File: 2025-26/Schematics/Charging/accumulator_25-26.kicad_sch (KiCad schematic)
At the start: 20 parts, among them J1 Conn_02x06_Counter_Clockwise, J2 Conn_02x06_Counter_Clockwise, K1 GV24 1BAX, K3 P115 BDA, K4 GV24 1BAX, U3 RSB, U5 Volt_indic

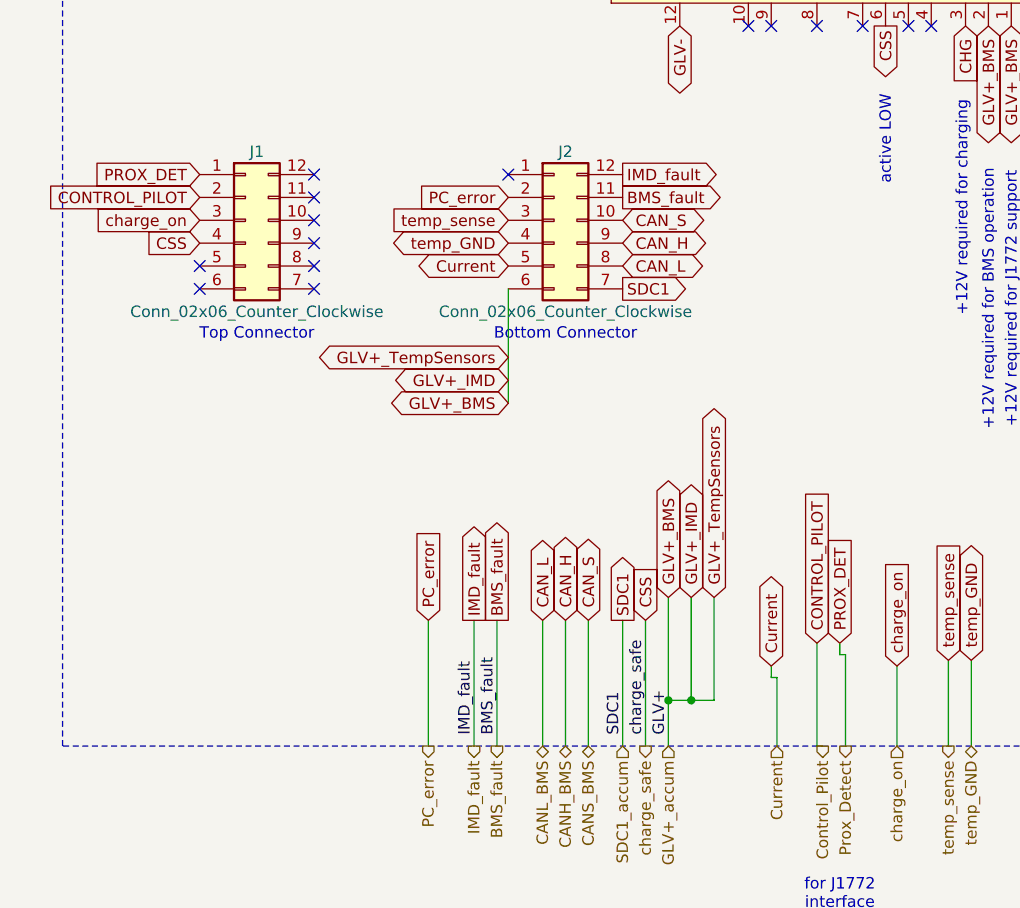
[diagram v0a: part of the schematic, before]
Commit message: updates to accumulator sch
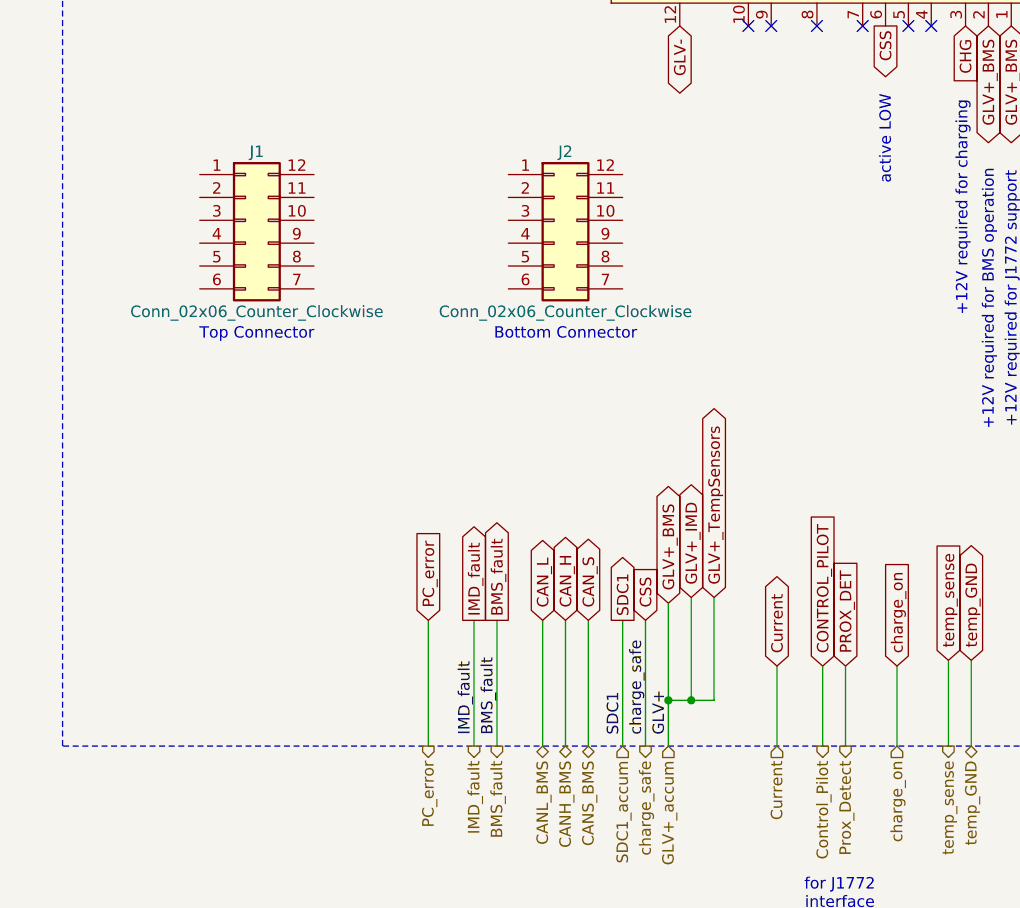
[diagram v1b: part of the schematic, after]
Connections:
- net BMS_fault: no longer J2.11 (Pin_11)
- net CAN_H: no longer J2.9 (Pin_9)
- net CAN_L: no longer J2.8 (Pin_8)
- net CAN_S: no longer J2.10 (Pin_10)
- net CONTROL_PILOT: no longer J1.2 (Pin_2)
- net CSS: no longer J1.4 (Pin_4)
- net Current: no longer J2.5 (Pin_5)
- net GLV+: no longer J2.6 (Pin_6)
- net IMD_fault: no longer J2.12 (Pin_12)
- net PC_error: no longer J2.2 (Pin_2)
- net PROX_DET: no longer J1.1 (Pin_1)
- net SDC1: no longer J2.7 (Pin_7)
- net charge_on: no longer J1.3 (Pin_3)
- net temp_GND: no longer J2.4 (Pin_4)
- net temp_sense: no longer J2.3 (Pin_3)
- net at U?. (Tap[1:8]): now also U1. (Taps[61:80]); no longer U?. (GND_Lug)
- new net: U?. (GND_Lug), U?. (Tap[1:8])
- no-connect marks 24 -> 15
